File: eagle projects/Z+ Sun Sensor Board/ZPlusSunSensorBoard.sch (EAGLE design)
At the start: 53 parts, among them U2 ADS7841E_2K5, U4 LM20BIM7X_NOPB, U6 TLV9051IDCKR, U8 TLV9051IDCKR, U9 TLV9051IDCKR

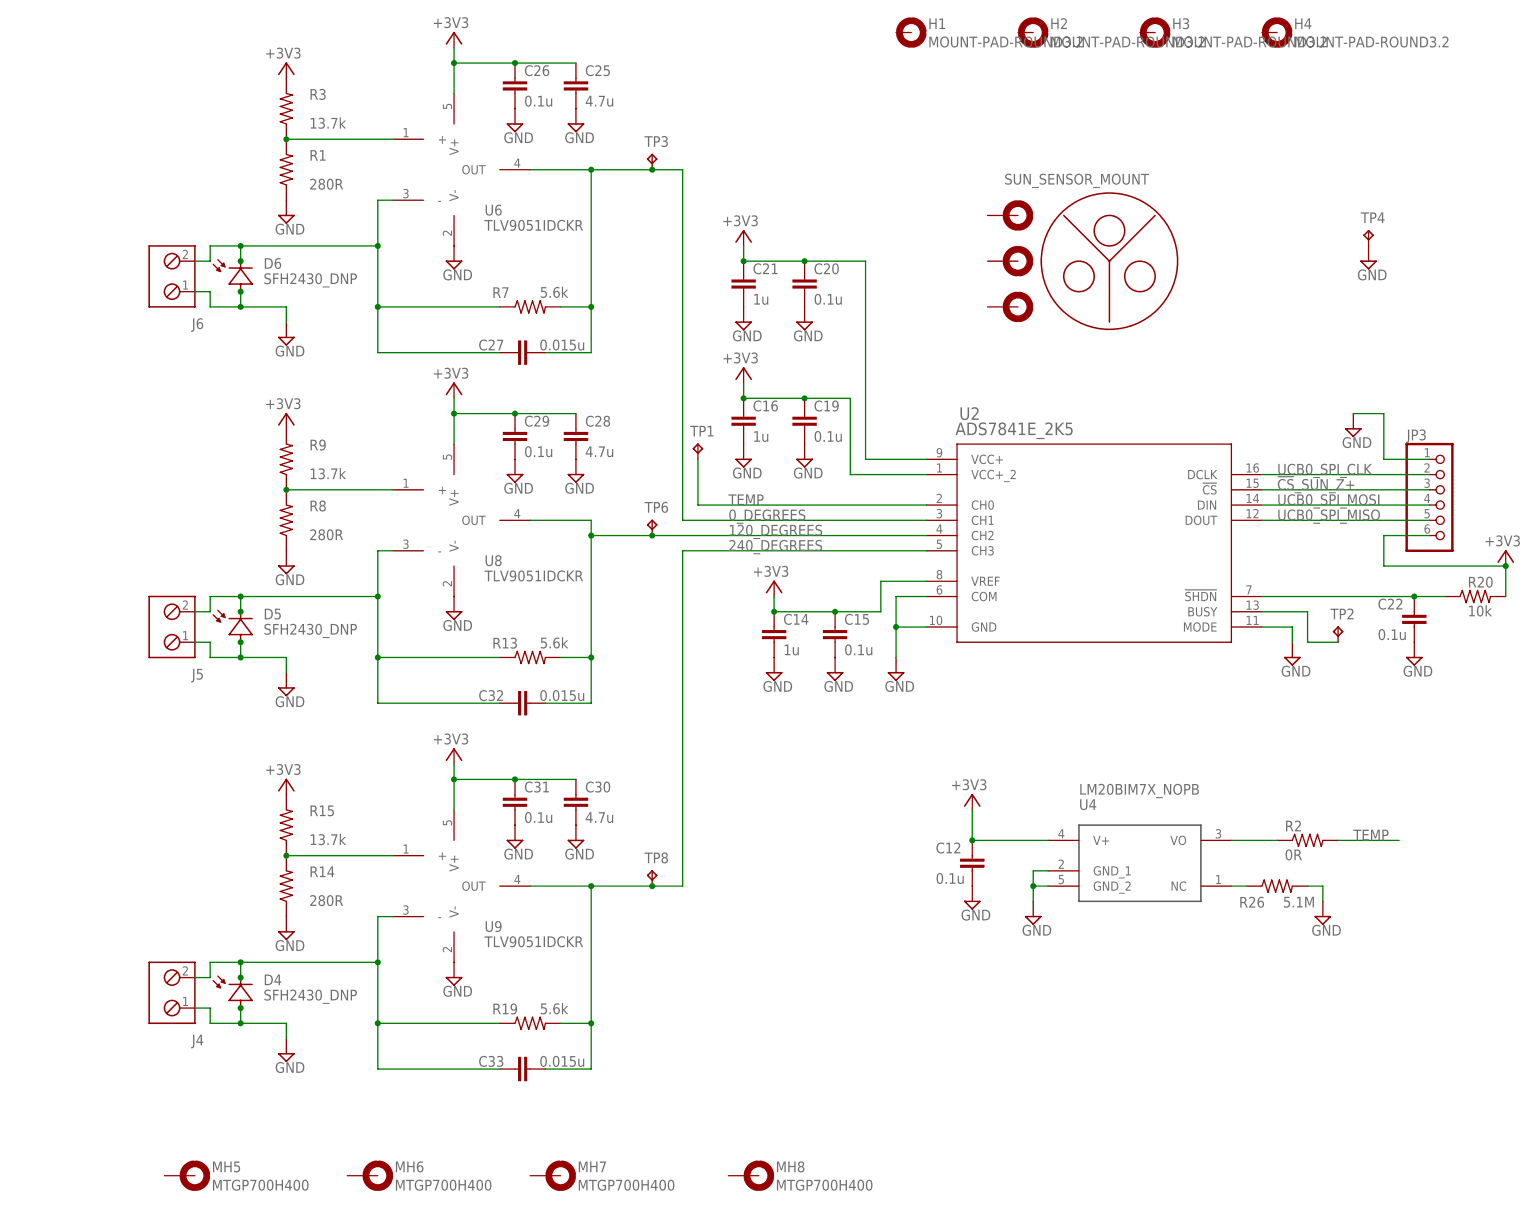
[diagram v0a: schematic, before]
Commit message: updates to Z+ sun sense board for 3d models
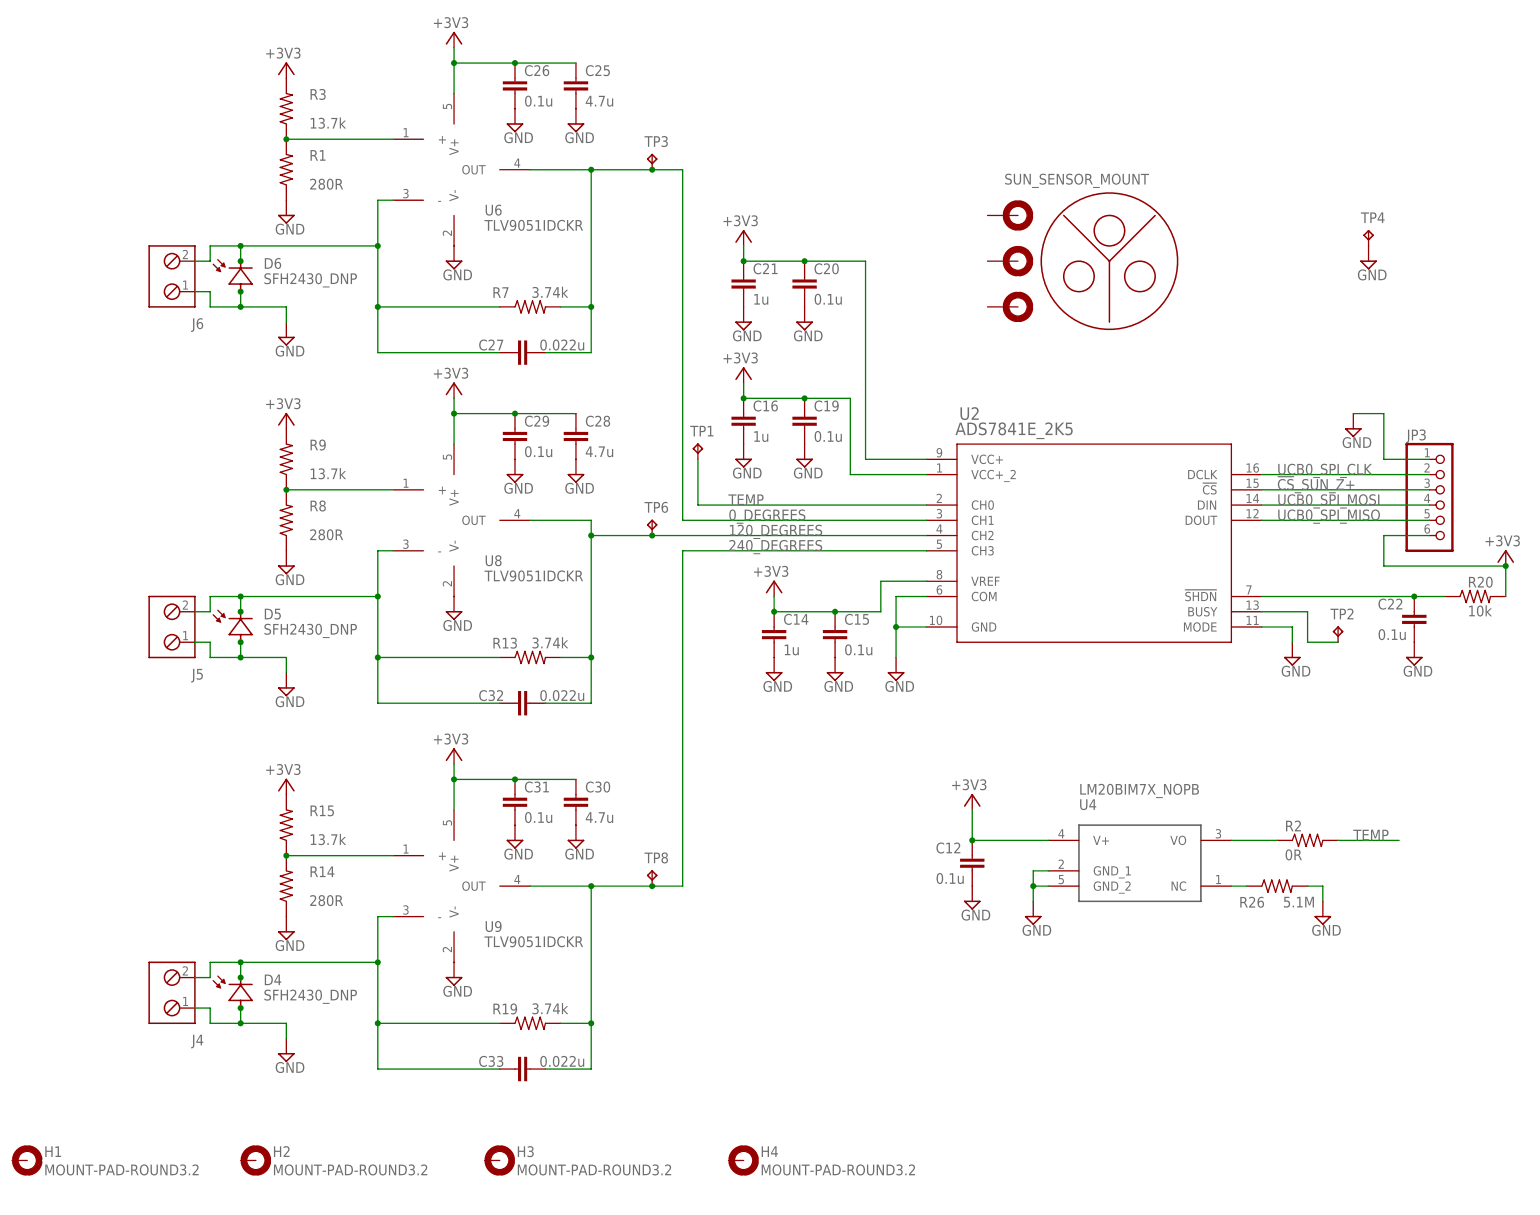
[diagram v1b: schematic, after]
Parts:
- removed MH5, MH6, MH7, MH8: MTGP700H400, my_library:MTGP700H400
- C12: device rcl:C-EUC0603 -> rcl:C-EUC0402
- C27, C32, C33: value 0.015u -> 0.022u
- R13, R19, R7: value 5.6k -> 3.74k
- R26: device rcl:R-US_R0603 -> rcl:R-US_R0402
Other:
- moved on the sheet: H1, H2, H3, H4

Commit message: Finalized sun sense board
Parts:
- H1, H2, H3, H4: value MOUNT-PAD-ROUND3.2 -> MOUNT-PAD-ROUND; device holes:MOUNT-PAD-ROUND3.2 -> my_library:MOUNT-PAD-ROUND
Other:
- note added: "A"
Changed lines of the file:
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@@
 <layer number="111" name="LPC17xx" color="7" fill="1" visible="yes" active="yes"/>
 <layer number="112" name="tSilk" color="7" fill="1" visible="yes" active="yes"/>
+<layer number="113" name="ReferenceLS" color="7" fill="1" visible="no" active="no"/>
 <layer number="116" name="Patch_BOT" color="9" fill="4" visible="yes" active="yes"/>
 <layer number="118" name="Rect_Pads" color="7" fill="1" visible="no" active="no"/>
@@
 <schematic xreflabel="%F%N" xrefpart="/%S.%C%R">
 <attributes>
-<attribute name="REV#" value="A"/>
+<attribute name="DESIGNER" value="T. Christison"/>
 </attributes>
 <variantdefs>
@@
 <part name="SUPPLY1" library="supply2" library_urn="urn:adsk.eagle:library:372" deviceset="GND" device=""/>
 <part name="SUPPLY2" library="supply2" library_urn="urn:adsk.eagle:library:372" deviceset="GND" device=""/>
-<part name="H1" library="holes" library_urn="urn:adsk.eagle:library:237" deviceset="MOUNT-PAD-ROUND" device="3.2" package3d_urn="urn:adsk.eagle:package:14282/1"/>
-<part name="H2" library="holes" library_urn="urn:adsk.eagle:library:237" deviceset="MOUNT-PAD-ROUND" device="3.2" package3d_urn="urn:adsk.eagle:package:14282/1"/>
-<part name="H3" library="holes" library_urn="urn:adsk.eagle:library:237" deviceset="MOUNT-PAD-ROUND" device="3.2" package3d_urn="urn:adsk.eagle:package:14282/1"/>
-<part name="H4" library="holes" library_urn="urn:adsk.eagle:library:237" deviceset="MOUNT-PAD-ROUND" device="3.2" package3d_urn="urn:adsk.eagle:package:14282/1"/>
+<part name="H1" library="my_library" library_urn="urn:adsk.eagle:library:22876504" deviceset="MOUNT-PAD-ROUND" device="" package3d_urn="urn:adsk.eagle:package:26858043/1"/>
+<part name="H2" library="my_library" library_urn="urn:adsk.eagle:library:22876504" deviceset="MOUNT-PAD-ROUND" device="" package3d_urn="urn:adsk.eagle:package:26858043/1"/>
+<part name="H3" library="my_library" library_urn="urn:adsk.eagle:library:22876504" deviceset="MOUNT-PAD-ROUND" device="" package3d_urn="urn:adsk.eagle:package:26858043/1"/>
+<part name="H4" library="my_library" library_urn="urn:adsk.eagle:library:22876504" deviceset="MOUNT-PAD-ROUND" device="" package3d_urn="urn:adsk.eagle:package:26858043/1"/>
 <part name="TP4" library="my_library" library_urn="urn:adsk.eagle:library:22876504" deviceset="TESTPOINT" device="" package3d_urn="urn:adsk.eagle:package:24605432/2"/>
 <part name="FRAME1" library="my_library" library_urn="urn:adsk.eagle:library:22876504" deviceset="TITLE_BLOCK_LETTER" device="">
+<attribute name="DESIGNER" value=""/>
 <attribute name="REV#" value=""/>
 </part>
@@
 <sheet>
 <plain>
+<text x="262.128" y="7.112" size="2.54" layer="94">A</text>
 </plain>
 <instances>
@@
 <attribute name="DRAWING_NAME" x="190.5" y="19.05" size="2.54" layer="94"/>
 <attribute name="REV#" x="261.62" y="7.62" size="2.54" layer="94"/>
+<attribute name="DESIGNER" x="196.85" y="11.43" size="2.54" layer="94"/>
 </instance>
 </instances>

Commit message: Minor gerber updates to copper
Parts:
- JP3: device pinhead:PINHD-1X6 -> my_library:PINHD-1X6
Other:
- note added: "T. Christison"
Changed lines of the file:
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@@
 <part name="SUPPLY30" library="supply2" library_urn="urn:adsk.eagle:library:372" deviceset="GND" device=""/>
 <part name="SUPPLY31" library="supply2" library_urn="urn:adsk.eagle:library:372" deviceset="GND" device=""/>
-<part name="TP1" library="my_library" library_urn="urn:adsk.eagle:library:22876504" deviceset="TESTPOINT" device="" package3d_urn="urn:adsk.eagle:package:24605432/2"/>
+<part name="TP1" library="my_library" library_urn="urn:adsk.eagle:library:22876504" deviceset="TESTPOINT" device="" package3d_urn="urn:adsk.eagle:package:24605432/3"/>
 <part name="C22" library="resistor" library_urn="urn:adsk.eagle:library:348" deviceset="C-EU" device="C0402" package3d_urn="urn:adsk.eagle:package:23626/2" value="0.1u"/>
 <part name="SUPPLY32" library="supply2" library_urn="urn:adsk.eagle:library:372" deviceset="GND" device=""/>
@@
 <part name="R3" library="resistor" library_urn="urn:adsk.eagle:library:348" deviceset="R-US_" device="R0402" package3d_urn="urn:adsk.eagle:package:26058/2" value="13.7k"/>
 <part name="SUPPLY40" library="supply2" library_urn="urn:adsk.eagle:library:372" deviceset="GND" device=""/>
-<part name="TP3" library="my_library" library_urn="urn:adsk.eagle:library:22876504" deviceset="TESTPOINT" device="" package3d_urn="urn:adsk.eagle:package:24605432/2"/>
+<part name="TP3" library="my_library" library_urn="urn:adsk.eagle:library:22876504" deviceset="TESTPOINT" device="" package3d_urn="urn:adsk.eagle:package:24605432/3"/>
 <part name="U6" library="my_library" library_urn="urn:adsk.eagle:library:22876504" deviceset="TLV9051" device="IDCKR" package3d_urn="urn:adsk.eagle:package:25994724/2"/>
 <part name="SUPPLY41" library="supply2" library_urn="urn:adsk.eagle:library:372" deviceset="GND" device=""/>
@@
 <part name="R9" library="resistor" library_urn="urn:adsk.eagle:library:348" deviceset="R-US_" device="R0402" package3d_urn="urn:adsk.eagle:package:26058/2" value="13.7k"/>
 <part name="SUPPLY44" library="supply2" library_urn="urn:adsk.eagle:library:372" deviceset="GND" device=""/>
-<part name="TP6" library="my_library" library_urn="urn:adsk.eagle:library:22876504" deviceset="TESTPOINT" device="" package3d_urn="urn:adsk.eagle:package:24605432/2"/>
+<part name="TP6" library="my_library" library_urn="urn:adsk.eagle:library:22876504" deviceset="TESTPOINT" device="" package3d_urn="urn:adsk.eagle:package:24605432/3"/>
 <part name="U8" library="my_library" library_urn="urn:adsk.eagle:library:22876504" deviceset="TLV9051" device="IDCKR" package3d_urn="urn:adsk.eagle:package:25994724/2"/>
 <part name="SUPPLY45" library="supply2" library_urn="urn:adsk.eagle:library:372" deviceset="GND" device=""/>
@@
 <part name="R15" library="resistor" library_urn="urn:adsk.eagle:library:348" deviceset="R-US_" device="R0402" package3d_urn="urn:adsk.eagle:package:26058/2" value="13.7k"/>
 <part name="SUPPLY49" library="supply2" library_urn="urn:adsk.eagle:library:372" deviceset="GND" device=""/>
-<part name="TP8" library="my_library" library_urn="urn:adsk.eagle:library:22876504" deviceset="TESTPOINT" device="" package3d_urn="urn:adsk.eagle:package:24605432/2"/>
+<part name="TP8" library="my_library" library_urn="urn:adsk.eagle:library:22876504" deviceset="TESTPOINT" device="" package3d_urn="urn:adsk.eagle:package:24605432/3"/>
 <part name="U9" library="my_library" library_urn="urn:adsk.eagle:library:22876504" deviceset="TLV9051" device="IDCKR" package3d_urn="urn:adsk.eagle:package:25994724/2"/>
 <part name="SUPPLY50" library="supply2" library_urn="urn:adsk.eagle:library:372" deviceset="GND" device=""/>
@@
 <part name="+3V21" library="supply1" library_urn="urn:adsk.eagle:library:371" deviceset="+3V3" device=""/>
 <part name="R20" library="resistor" library_urn="urn:adsk.eagle:library:348" deviceset="R-US_" device="R0402" package3d_urn="urn:adsk.eagle:package:26058/2" value="10k"/>
-<part name="J4" library="my_library" library_urn="urn:adsk.eagle:library:22876504" deviceset="TRM_BLK_1X2" device="" package3d_urn="urn:adsk.eagle:package:9320/1"/>
+<part name="J4" library="my_library" library_urn="urn:adsk.eagle:library:22876504" deviceset="TRM_BLK_1X2" device="" package3d_urn="urn:adsk.eagle:package:26488321/3"/>
 <part name="D4" library="my_library" library_urn="urn:adsk.eagle:library:22876504" deviceset="SFH2430_DNP" device=""/>
 <part name="SUPPLY51" library="supply2" library_urn="urn:adsk.eagle:library:372" deviceset="GND" device=""/>
-<part name="J5" library="my_library" library_urn="urn:adsk.eagle:library:22876504" deviceset="TRM_BLK_1X2" device="" package3d_urn="urn:adsk.eagle:package:9320/1"/>
+<part name="J5" library="my_library" library_urn="urn:adsk.eagle:library:22876504" deviceset="TRM_BLK_1X2" device="" package3d_urn="urn:adsk.eagle:package:26488321/3"/>
 <part name="D5" library="my_library" library_urn="urn:adsk.eagle:library:22876504" deviceset="SFH2430_DNP" device=""/>
 <part name="SUPPLY52" library="supply2" library_urn="urn:adsk.eagle:library:372" deviceset="GND" device=""/>
-<part name="J6" library="my_library" library_urn="urn:adsk.eagle:library:22876504" deviceset="TRM_BLK_1X2" device="" package3d_urn="urn:adsk.eagle:package:9320/1"/>
+<part name="J6" library="my_library" library_urn="urn:adsk.eagle:library:22876504" deviceset="TRM_BLK_1X2" device="" package3d_urn="urn:adsk.eagle:package:26488321/3"/>
 <part name="D6" library="my_library" library_urn="urn:adsk.eagle:library:22876504" deviceset="SFH2430_DNP" device=""/>
 <part name="+3V1" library="supply1" library_urn="urn:adsk.eagle:library:371" deviceset="+3V3" device=""/>
 <part name="R2" library="rcl" library_urn="urn:adsk.eagle:library:334" deviceset="R-US_" device="R0805" package3d_urn="urn:adsk.eagle:package:23553/2" value="0R"/>
-<part name="TP2" library="my_library" library_urn="urn:adsk.eagle:library:22876504" deviceset="TESTPOINT" device="" package3d_urn="urn:adsk.eagle:package:24605432/2"/>
+<part name="TP2" library="my_library" library_urn="urn:adsk.eagle:library:22876504" deviceset="TESTPOINT" device="" package3d_urn="urn:adsk.eagle:package:24605432/3"/>
 <part name="A1" library="my_library" library_urn="urn:adsk.eagle:library:22876504" deviceset="SUN_SENSOR_MOUNT" device="" package3d_urn="urn:adsk.eagle:package:26239251/3"/>
-<part name="JP3" library="pinhead" library_urn="urn:adsk.eagle:library:325" deviceset="PINHD-1X6" device="" package3d_urn="urn:adsk.eagle:package:22472/2"/>
+<part name="JP3" library="my_library" library_urn="urn:adsk.eagle:library:22876504" deviceset="PINHD-1X6" device="" package3d_urn="urn:adsk.eagle:package:26872615/1"/>
 <part name="SUPPLY1" library="supply2" library_urn="urn:adsk.eagle:library:372" deviceset="GND" device=""/>
 <part name="SUPPLY2" library="supply2" library_urn="urn:adsk.eagle:library:372" deviceset="GND" device=""/>
@@
 <part name="H3" library="my_library" library_urn="urn:adsk.eagle:library:22876504" deviceset="MOUNT-PAD-ROUND" device="" package3d_urn="urn:adsk.eagle:package:26858043/1"/>
 <part name="H4" library="my_library" library_urn="urn:adsk.eagle:library:22876504" deviceset="MOUNT-PAD-ROUND" device="" package3d_urn="urn:adsk.eagle:package:26858043/1"/>
-<part name="TP4" library="my_library" library_urn="urn:adsk.eagle:library:22876504" deviceset="TESTPOINT" device="" package3d_urn="urn:adsk.eagle:package:24605432/2"/>
+<part name="TP4" library="my_library" library_urn="urn:adsk.eagle:library:22876504" deviceset="TESTPOINT" device="" package3d_urn="urn:adsk.eagle:package:24605432/3"/>
 <part name="FRAME1" library="my_library" library_urn="urn:adsk.eagle:library:22876504" deviceset="TITLE_BLOCK_LETTER" device="">
 <attribute name="DESIGNER" value=""/>
@@
 <plain>
 <text x="262.128" y="7.112" size="2.54" layer="94">A</text>
+<text x="190.754" y="11.43" size="2.54" layer="94">T. Christison</text>
 </plain>
 <instances>

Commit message: bfwebfibc
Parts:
- added R4: 5.1M, resistor:R-US_R0402
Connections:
- net GND: now also R4.1
- net N$2: now also R4.2
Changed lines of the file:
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@@
 <attribute name="REV#" value=""/>
 </part>
+<part name="R4" library="resistor" library_urn="urn:adsk.eagle:library:348" deviceset="R-US_" device="R0402" package3d_urn="urn:adsk.eagle:package:26058/2" value="5.1M"/>
+<part name="SUPPLY3" library="supply2" library_urn="urn:adsk.eagle:library:372" deviceset="GND" device=""/>
 </parts>
 <sheets>
@@
 <attribute name="DESIGNER" x="196.85" y="11.43" size="2.54" layer="94"/>
 </instance>
+<instance part="R4" gate="G$1" x="233.68" y="93.98" smashed="yes" rot="R90">
+<attribute name="NAME" x="232.1814" y="92.71" size="1.778" layer="95" rot="R90"/>
+<attribute name="VALUE" x="236.982" y="92.71" size="1.778" layer="96" rot="R90"/>
+</instance>
+<instance part="SUPPLY3" gate="GND" x="233.68" y="86.36" smashed="yes">
+<attribute name="VALUE" x="231.775" y="83.185" size="1.778" layer="96"/>
+</instance>
 </instances>
 <busses>
@@
 <pinref part="SUPPLY2" gate="GND" pin="GND"/>
 <pinref part="TP4" gate="G$1" pin="TP"/>
+</segment>
+<segment>
+<pinref part="R4" gate="G$1" pin="1"/>
+<pinref part="SUPPLY3" gate="GND" pin="GND"/>
 </segment>
 </net>
@@
 <pinref part="TP2" gate="G$1" pin="TP"/>
 <wire x1="228.6" y1="99.06" x2="233.68" y2="99.06" width="0.1524" layer="91"/>
-</segment>
-</net>
+<pinref part="R4" gate="G$1" pin="2"/>
+<junction x="233.68" y="99.06"/>
+</segment>
+</net>
